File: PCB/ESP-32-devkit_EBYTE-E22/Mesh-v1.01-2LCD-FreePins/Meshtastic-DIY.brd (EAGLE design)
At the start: 97.8 x 55.9 mm, 24 parts

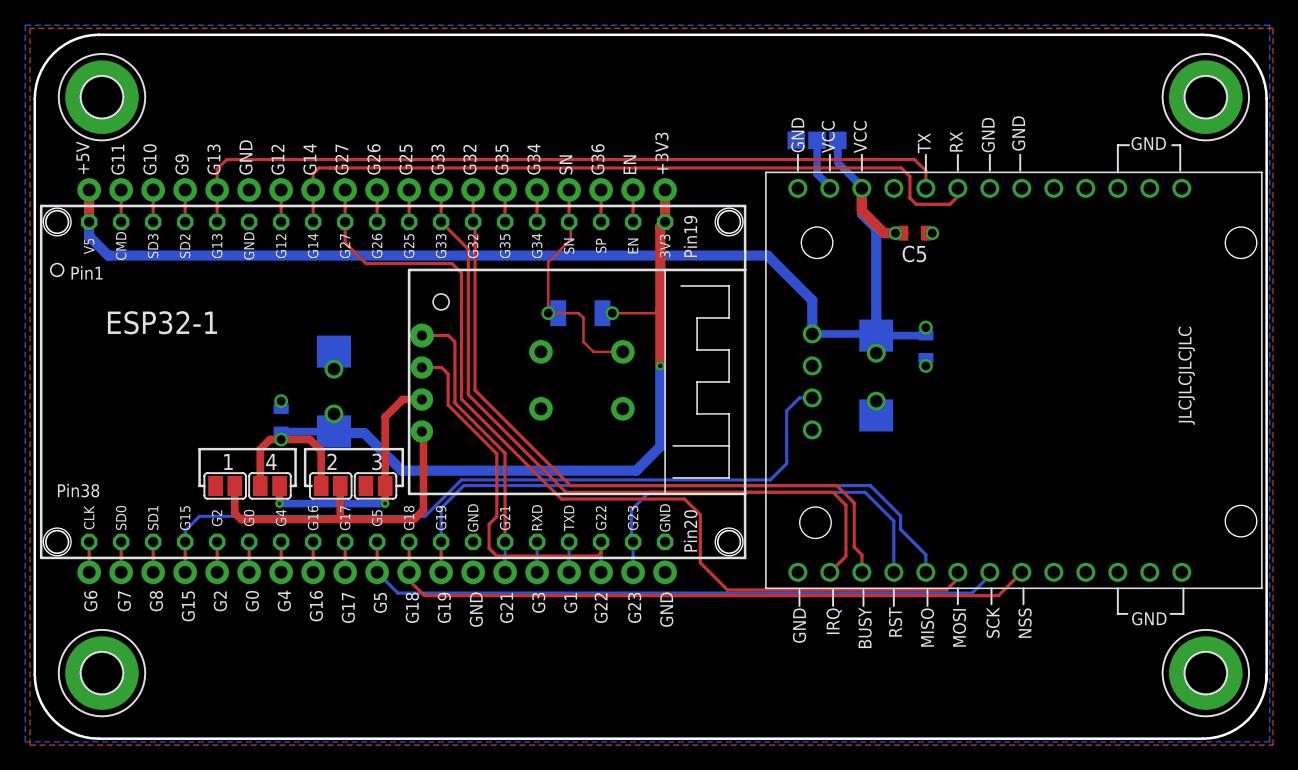
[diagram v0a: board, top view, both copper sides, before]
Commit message: PCB updates (#15)
* fixes PCB version and description

* Updated revision of the v1.01 PCB

* Fixed drill layout for v.1.05

* Updated EBYTE E22 adapter (removed excessive antenna line)

* Updated PCB v1.03

* Updated PCB v1.02

* Removed untested PCB design

* [PCB] Missing brd&sch for 1.01 & updated 1.02

* v1.04 update

* [PCB] Meshtastic-DIY_v1.06 - TTGO T-Energy T18 V3.0 HAT
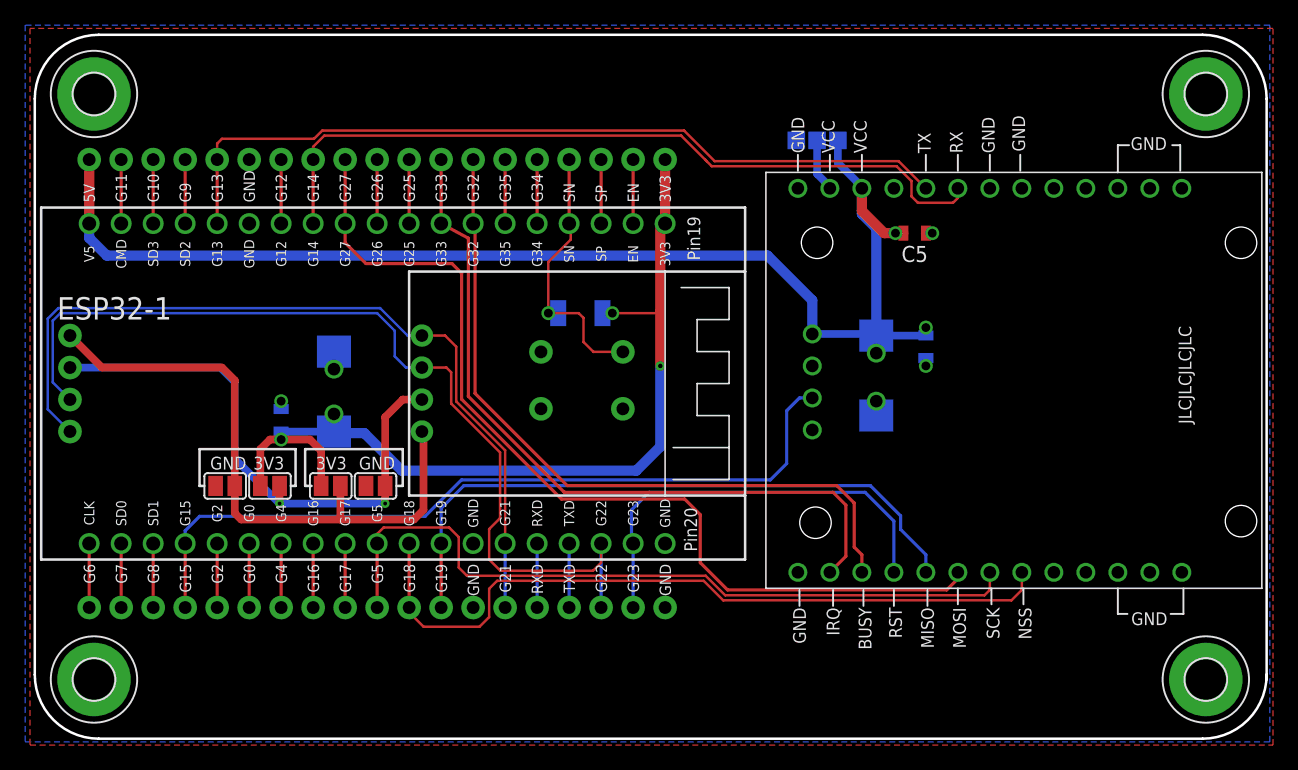
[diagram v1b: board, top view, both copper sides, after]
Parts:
- added J3: (no value), SparkFun-Connectors:1X04_NO_SILK
- moved ESP32-1 3.98 mm to (28.4, 28.2)
- moved J2 2.79 mm to (4.32, 10.4)
- moved J1 2.41 mm to (4.32, 46.0)
- moved H3 0.81 mm to (4.70, 4.70)
- moved H1 0.68 mm to (4.70, 51.2)
- moved H4 0.51 mm to (93.0, 4.70)
- moved H2 0.25 mm to (93.0, 51.2)
- renumbered 1 to GND, 4 to 3V3
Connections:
- net LCD_SCK: now also J3.3
- net LCD_SDA: now also J3.4
- net N$2: now also J3.2
- net N$4: now also J3.1
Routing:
- net LCD_SCK: track 30.5 -> 74.8 mm
- net LCD_SDA: track 22.8 -> 66.0 mm
- net N$2: track 20.1 -> 44.8 mm
- net N$4: track 26.6 -> 49.5 mm
- net SCK: track 52.6 -> 59.9 mm
- net NSS: track 53.0 -> 59.8 mm
- net RXEN: track 58.3 -> 61.6 mm
- net IRQ: track 56.6 -> 59.5 mm
- net RST: track 31.4 -> 34.3 mm
- net MISO: track 48.6 -> 51.4 mm
- net +3V3: track 70.0 -> 72.7 mm
- net BUSY: track 55.5 -> 58.2 mm
- net G8: track 2.41 -> 5.08 mm
- net G7: track 2.41 -> 5.08 mm
- net G6: track 2.41 -> 5.08 mm
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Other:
- board text added: "3V3"
- board text added: "RXD"
- board text added: "SP"
- board text added: "TXD"
- board text removed: "+3V3"
- board text removed: "+5V"
- board text removed: "G1"
- board text removed: "G3"
- board text removed: "G36"
